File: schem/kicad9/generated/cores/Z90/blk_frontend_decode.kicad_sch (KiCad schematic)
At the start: 0 parts

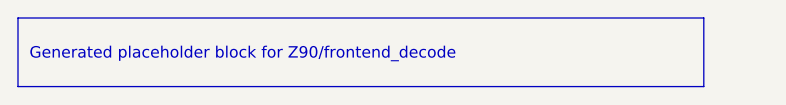
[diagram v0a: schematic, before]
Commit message: kicad: generate core-level hierarchical schematics
Detailed description:
- What changed: regenerated common and core schematics for Z85/Z90/Z380/Z480, Am9513/4/5, Am95xx, and CarbonIO/DMA placeholders
- Why it changed: update generated KiCad 9 outputs to reflect the final naming and tier model
- Files/paths affected: schem/kicad9/generated/common/* and schem/kicad9/generated/cores/*
- How to run it: scripts/gen_kicad.sh (or python tools/kicadgen/src/kicadgen.py)
- What remains TODO: regenerate and commit system-level schematics
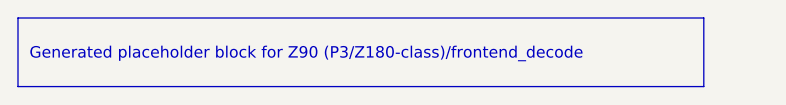
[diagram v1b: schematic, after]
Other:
- title: Z90::frontend_decode -> Z90 (P3/Z180-class)::frontend_decode
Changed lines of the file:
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@@
 	(version 20250114)
 	(generator "kicadgen")
-	(generator_version "0.1")
+	(generator_version "0.2")
 	(paper "A3")
 	(title_block
-		(title "Z90::frontend_decode")
+		(title "Z90 (P3/Z180-class)::frontend_decode")
 		(company "Project Carbon")
 		(comment 1 "Generated - do not edit in generated/")
@@
 	)
 	(text_box
-		"Generated placeholder block for Z90/frontend_decode"
+		"Generated placeholder block for Z90 (P3/Z180-class)/frontend_decode"
 		(exclude_from_sim no)
 		(at
